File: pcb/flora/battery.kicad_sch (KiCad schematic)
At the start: 43 parts, among them IC3 TP4056X, IC4 FS8205A, IC5 DW01+G, IC6 TPS54331DR, U2 AMS1117

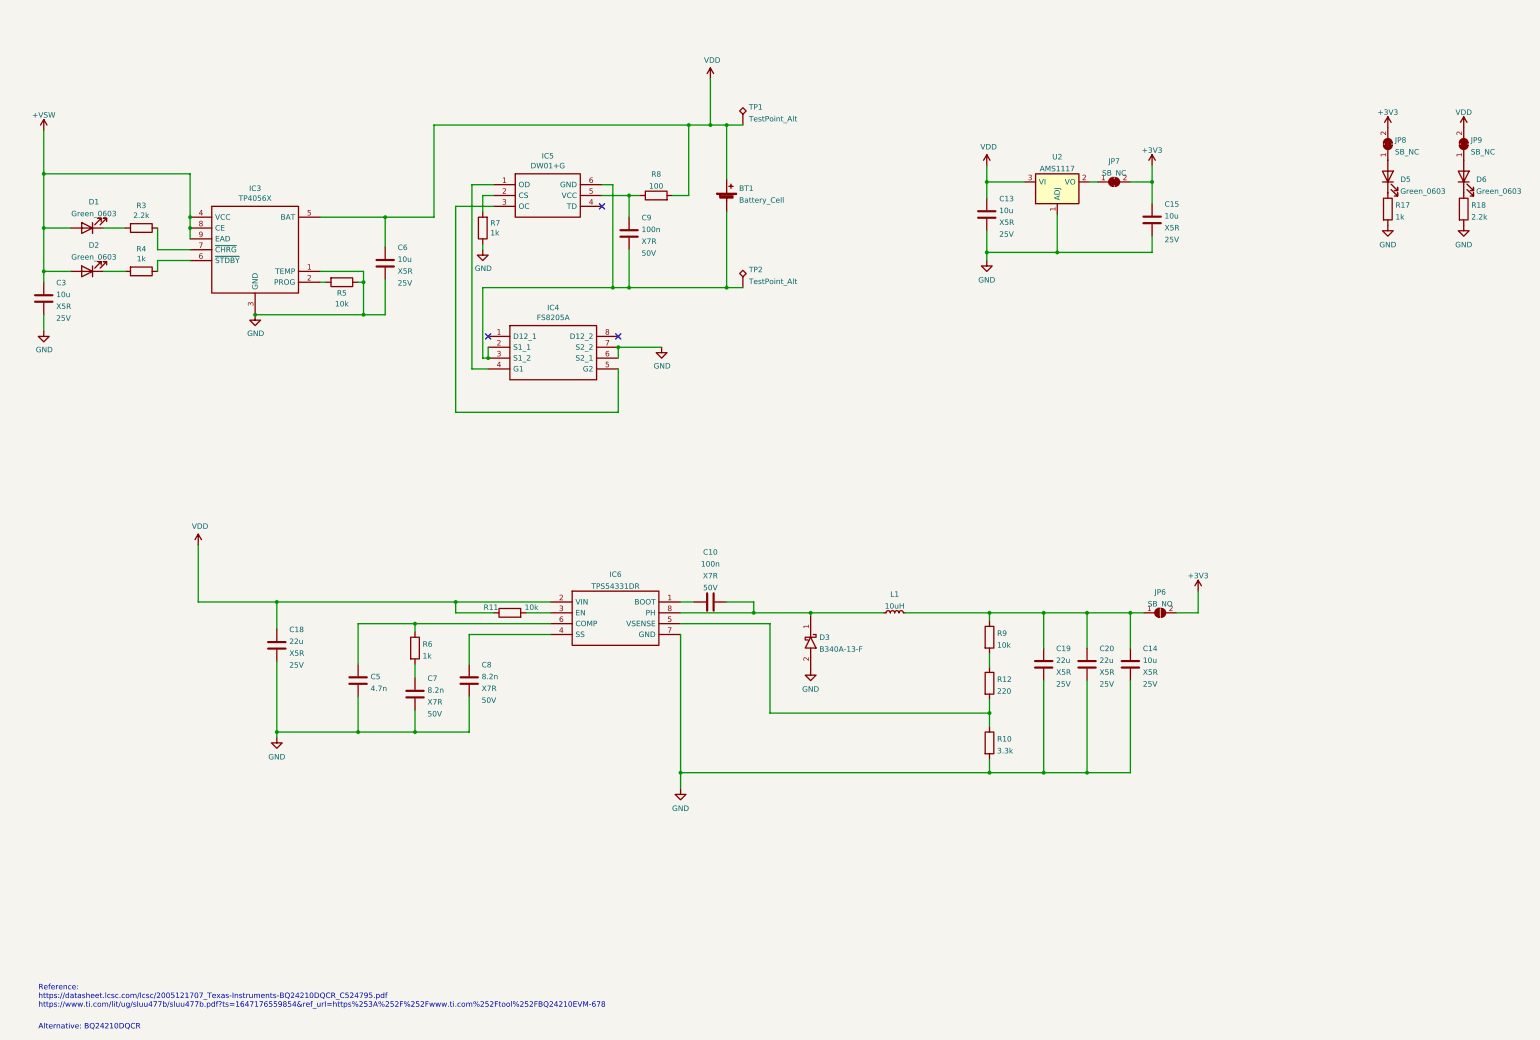
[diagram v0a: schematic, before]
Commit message: Added comments to power
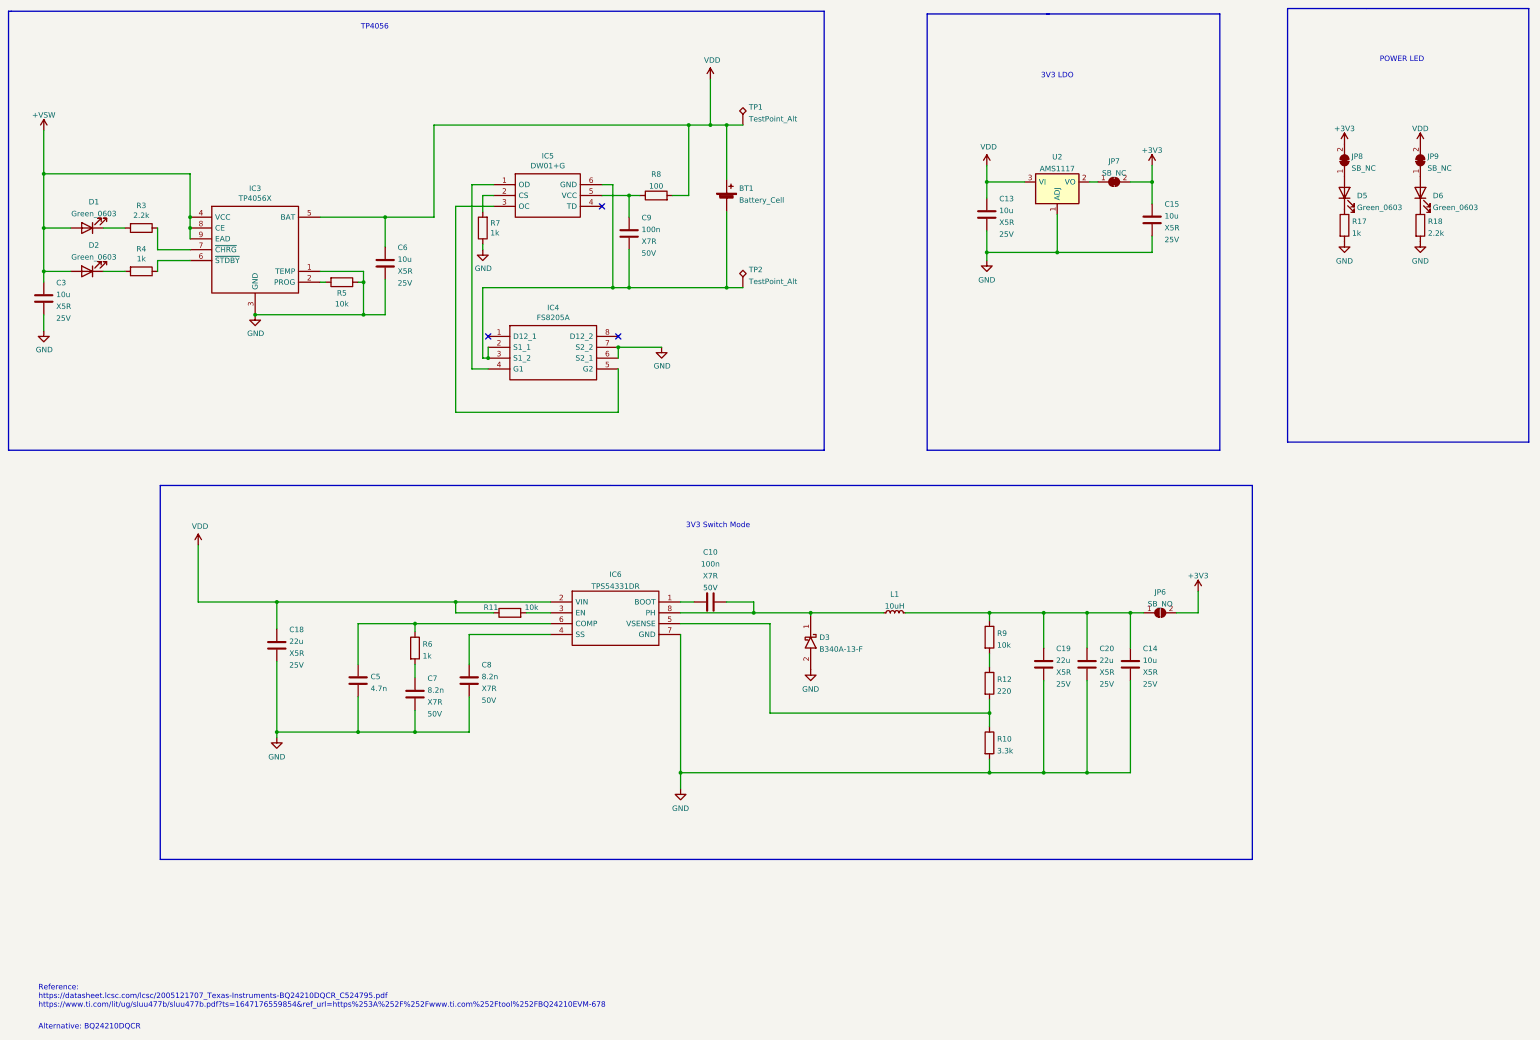
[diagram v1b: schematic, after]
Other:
- note added: "3V3 LDO"
- note added: "3V3 Switch Mode"
- note added: "POWER LED"
- note added: "TP4056"
- moved on the sheet: D5, D6, JP8, JP9, R17, R18

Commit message: released Rev A
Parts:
- removed U2: AMS1117, Package_TO_SOT_SMD:SOT-223-3_TabPin2, symbol Regulator_Linear:AMS1117
- added IC7: AMS1117-3.3, Package_TO_SOT_SMD:SOT-223-3_TabPin2, symbol Power-Drivers_JLC:AMS1117-3.3
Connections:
- net GND: now also IC7.1 (GND)
- net VDD: now also IC7.3 (VI)
- net at JP7.1 (A): now also IC7.2 (VO)
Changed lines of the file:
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@@
     (pin "2")
+  )
+  (symbol (lib_id "Power-Drivers_JLC:AMS1117-3.3") (at 280.67 75.565 0) (unit 1)
+    (in_bom yes) (on_board yes) (fields_autoplaced)
+    (property "Reference" "IC7" (id 0) (at 290.195 65.2485 0))
+    (property "Value" "AMS1117-3.3" (id 1) (at 290.195 68.0236 0))
+    (property "Footprint" "Package_TO_SOT_SMD:SOT-223-3_TabPin2" (id 2) (at 322.58 75.565 0)
+      (effects (font (size 1.27 1.27)) (justify left) hide)
+    )
+    (property "Datasheet" "http://www.advanced-monolithic.com/pdf/ds1117.pdf" (id 3) (at 322.58 78.105 0)
+      (effects (font (size 1.27 1.27)) (justify left) hide)
+    )
+    (property "Description" "1A LOW DROPOUT VOLTAGE REGULATOR, SOT-223" (id 4) (at 322.58 80.645 0)
+      (effects (font (size 1.27 1.27)) (justify left) hide)
+    )
+    (property "Height" "1.8" (id 5) (at 322.58 83.185 0)
+      (effects (font (size 1.27 1.27)) (justify left) hide)
+    )
+    (property "Manufacturer_Name" "Advanced Monolithic Systems" (id 6) (at 322.58 85.725 0)
+      (effects (font (size 1.27 1.27)) (justify left) hide)
+    )
+    (property "Manufacturer_Part_Number" "AMS1117-3.3" (id 7) (at 322.58 88.265 0)
+      (effects (font (size 1.27 1.27)) (justify left) hide)
+    )
+    (property "LCSC" "C6186" (id 8) (at 325.755 90.805 0)
+      (effects (font (size 1.27 1.27)) hide)
+    )
+    (pin "1")
+    (pin "2")
+    (pin "3")
   )
   (symbol (lib_id "Capacitor_JLC:4.7n") (at 126.365 187.96 0) (unit 1)
@@
     (pin "2")
   )
-  (symbol (lib_id "Regulator_Linear:AMS1117") (at 290.195 71.12 0) (unit 1)
-    (in_bom yes) (on_board yes) (fields_autoplaced)
-    (property "Reference" "U2" (id 0) (at 290.195 65.2485 0))
-    (property "Value" "AMS1117" (id 1) (at 290.195 68.0236 0))
-    (property "Footprint" "Package_TO_SOT_SMD:SOT-223-3_TabPin2" (id 2) (at 290.195 66.04 0)
-      (effects (font (size 1.27 1.27)) hide)
-    )
-    (property "Datasheet" "http://www.advanced-monolithic.com/pdf/ds1117.pdf" (id 3) (at 292.735 77.47 0)
-      (effects (font (size 1.27 1.27)) hide)
-    )
-    (pin "1")
-    (pin "2")
-    (pin "3")
-  )
   (symbol (lib_id "power:VDD") (at 208.915 46.99 0) (unit 1)

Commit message: added image
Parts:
- added C26: 220uF_E_LV, Capacitor_SMD:CP_Elec_6.3x5.4, symbol Capacitor_JLC:220uF_E_LV
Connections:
- net GND: now also R6.2, C26.2; no longer C7.2
- net at C14.1, C19.1, C20.1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: now also C26.1
- net at C5.1, IC6.6 (COMP): now also C7.1; no longer R6.1
- new net: C7.2, R6.1
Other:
- title: (none) -> FLORA
- moved on the sheet: C10, C14, C18, C19, C20, C5, C7, C8, D3, IC6, JP6, L1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

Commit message: commit backups
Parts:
- C18, C19, C20: LCSC C45783 -> C602037
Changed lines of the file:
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@@
     (pin "8")
   )
-  (symbol (lib_id "Capacitor_JLC:22u") (at 287.02 185.42 0) (unit 1)
+  (symbol (lib_name "22u_1") (lib_id "Capacitor_JLC:22u") (at 287.02 185.42 0) (unit 1)
     (in_bom yes) (on_board yes) (fields_autoplaced)
     (property "Reference" "C19" (id 0) (at 289.941 181.7364 0)
@@
       (effects (font (size 1.27 1.27)) (justify left))
     )
-    (property "LCSC" "C45783" (id 5) (at 287.02 185.42 0)
+    (property "LCSC" "C602037" (id 5) (at 287.02 185.42 0)
       (effects (font (size 1.27 1.27)) hide)
     )
@@
     (pin "1")
   )
-  (symbol (lib_id "Capacitor_JLC:22u") (at 297.18 185.42 0) (unit 1)
+  (symbol (lib_name "22u_2") (lib_id "Capacitor_JLC:22u") (at 297.18 185.42 0) (unit 1)
     (in_bom yes) (on_board yes) (fields_autoplaced)
     (property "Reference" "C20" (id 0) (at 300.101 181.7364 0)
@@
       (effects (font (size 1.27 1.27)) (justify left))
     )
-    (property "LCSC" "C45783" (id 5) (at 297.18 185.42 0)
+    (property "LCSC" "C602037" (id 5) (at 297.18 185.42 0)
       (effects (font (size 1.27 1.27)) hide)
     )
@@
       (effects (font (size 1.27 1.27)) (justify left))
     )
-    (property "LCSC" "C45783" (id 5) (at 107.95 181.61 0)
-      (effects (font (size 1.27 1.27)) hide)
-    )
+    (property "LCSC" "C602037" (id 5) (at 107.95 181.61 0)
+      (effects (font (size 1.27 1.27)) hide)
+    )

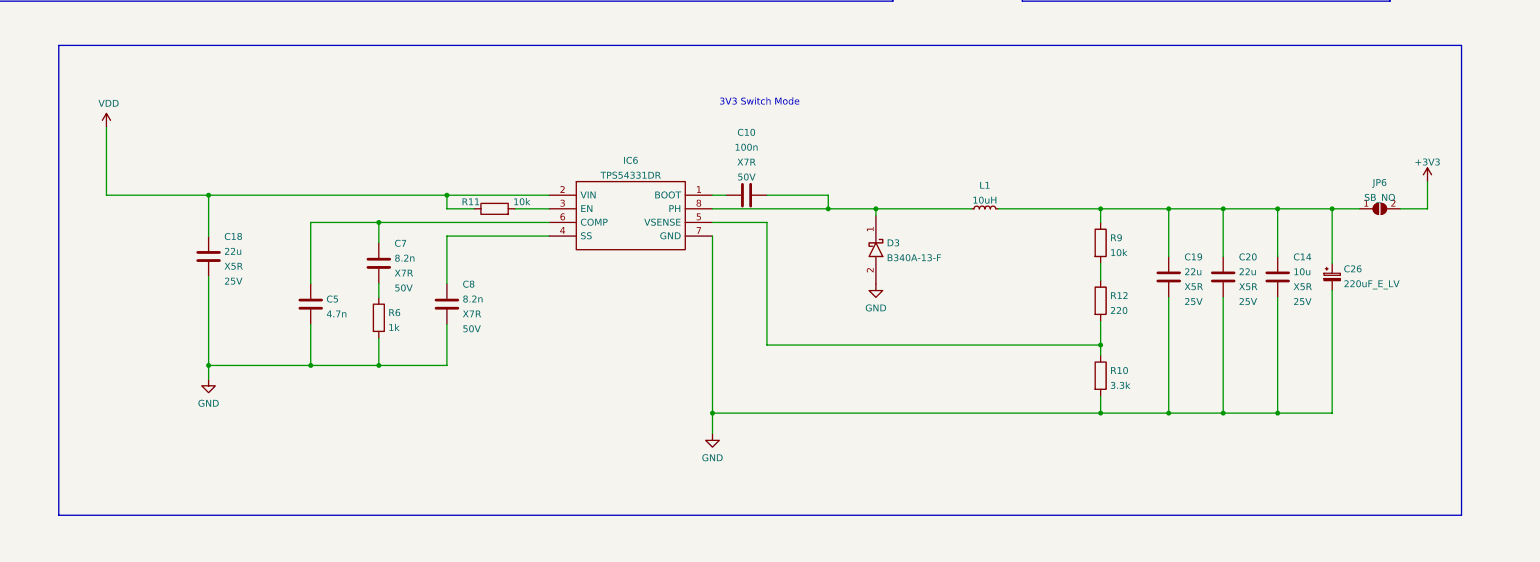
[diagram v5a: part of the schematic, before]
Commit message: Replaced SMPS
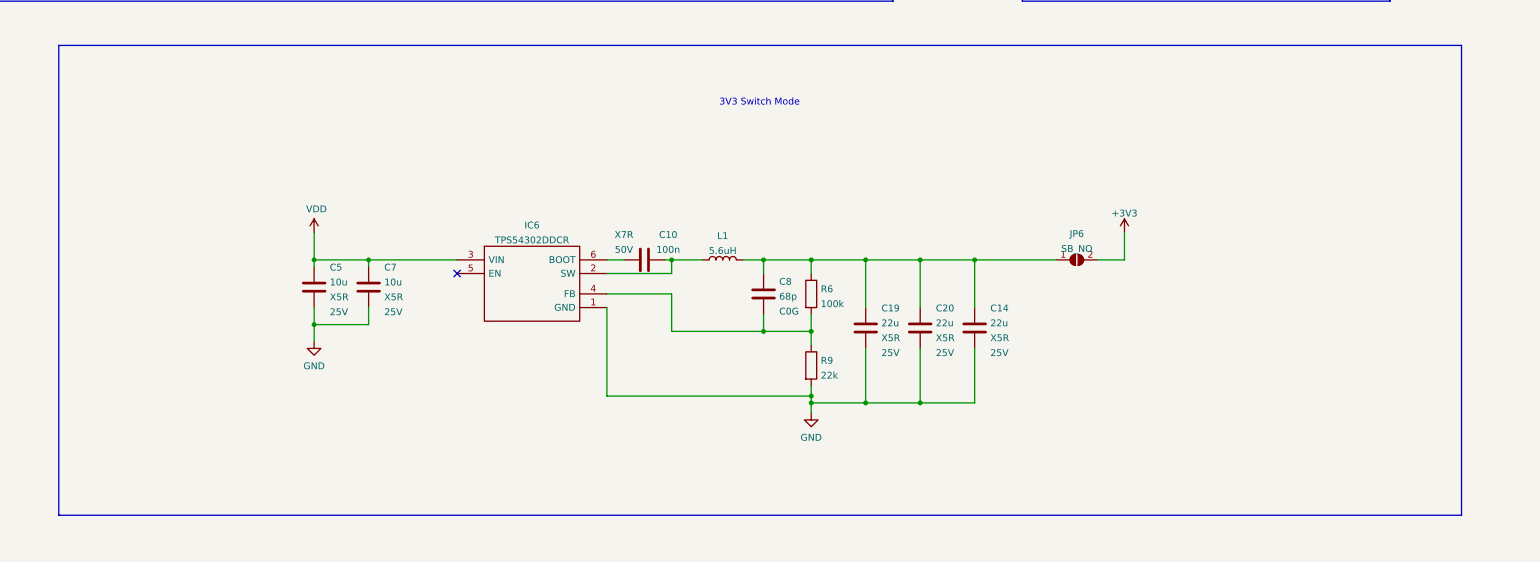
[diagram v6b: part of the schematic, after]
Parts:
- removed C14: 10u, Capacitor_SMD:C_0805_2012Metric, symbol Capacitor_JLC:10u
- removed C18: 22u, Capacitor_SMD:C_0805_2012Metric, symbol Capacitor_JLC:22u
- removed C26: 220uF_E_LV, Capacitor_SMD:CP_Elec_6.3x5.4, symbol Capacitor_JLC:220uF_E_LV
- removed C5: 4.7n, Capacitor_SMD:C_0402_1005Metric, symbol Capacitor_JLC:4.7n
- removed C7, C8: 8.2n, Capacitor_SMD:C_0402_1005Metric, symbol Capacitor_JLC:8.2n
- removed D3: B340A-13-F, DIOM5226X240N, symbol Diode_JLC:B340A-13-F
- removed IC6: TPS54331DR, SOIC127P600X175-8N, symbol Power-Drivers_JLC:TPS54331DR
- removed L1: 10uH, SamacSys_Parts:INDPM4040X300N, symbol Inductor_JLC:10uH
- removed R10: 3.3k, Resistor_SMD:R_0402_1005Metric, symbol Resistor_JLC:3.3k
- removed R11, R9: 10k, Resistor_SMD:R_0402_1005Metric, symbol Resistor_JLC:10k
- removed R12: 220, Resistor_SMD:R_0402_1005Metric, symbol Resistor_JLC:220
- removed R6: 1k, Resistor_SMD:R_0402_1005Metric, symbol Resistor_JLC:1k
- added C14: 22u, Capacitor_SMD:C_0805_2012Metric, symbol Capacitor_JLC:22u
- added C5, C7: 10u, Capacitor_SMD:C_0805_2012Metric, symbol Capacitor_JLC:10u
- added C8: 68p, Capacitor_SMD:C_0402_1005Metric, symbol Capacitor_JLC:68p
- added IC6: TPS54302DDCR, SOT95P280X110-6N, symbol Power-Drivers_JLC:TPS54302DDCR
- added L1: 5.6uH, SamacSys_Parts:INDPM4040X300N, symbol Inductor_JLC:5.6uH
- added R6: 100k, Resistor_SMD:R_0402_1005Metric, symbol Resistor_JLC:100k
- added R9: 22k, Resistor_SMD:R_0402_1005Metric, symbol Resistor_JLC:22k
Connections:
- net GND: now also C14.2, C5.2, C7.2, IC6.1 (GND), R9.2
- net VDD: now also C5.1, C7.1, IC6.3 (VIN)
- net at C19.1, C20.1, JP6.1 (A): now also C14.1, C8.1, L1.2, R6.1
- net at C10.2: now also IC6.2 (SW), L1.1
- net at C10.1: now also IC6.6 (BOOT)
- new net: C8.2, IC6.4 (FB), R6.2, R9.1
- no-connect marks 3 -> 4
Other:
- moved on the sheet: C10, C19, C20, JP6
